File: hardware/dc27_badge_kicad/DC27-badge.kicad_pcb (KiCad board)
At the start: 4 copper layers, 79.1 x 184.5 mm, 141 parts, among them J101 Conn_ARM_JTAG_SWD_10, J102 ShittyAddOnL, J103 ShittyAddOnR, J104 Conn_02x20_Odd_Even, J601 USB_MICRO_RIGHT, Q401 FDN360P, SW108 RESET, SW401 POWER ON, SW801 SKRHAAE010, SW802 SKRHAAE010, U100 BMD-340-A-R-DC27-peripheral-c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, U301 IS31FL3216A, U401 MCP73833, U402 LM1117-3.3, U501 CS4344-CZZ, U502 LM4880, U601 CP2102N-A01-GQFN28, U602 TPD3E001DRLR, Y101 32.768Khz XTAL

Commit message: update gerbers for R302 issue
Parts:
- H701: value MountingHole-Mechanical -> Bomb Face
- R302: footprint Resistor_SMD:R_0603_1608Metric -> Resistor_SMD:R_0805_2012Metric
- U301: value IS31FL3216A -> IS31FL3736-QFLS4-TR
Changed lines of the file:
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@@
     (add_net ~RESET_TGTMCU)
   )
+  (module Resistor_SMD:R_0805_2012Metric (layer F.Cu)
+    (at 108.5125 200)
+    (descr "Resistor SMD 0805 (2012 Metric), square (rectangular) end terminal, IPC_7351 nominal, (Body size source: https://docs.google.com/spreadsheets/d/1BsfQQcO9C6DZCsRaXUlFlo91Tg2WpOkGARC1WS5S8t0/edit?usp=sharing), generated with kicad-footprint-generator")
+    (tags resistor)
+    (attr smd)
+    (fp_text reference R302 (at 0 -1.65) (layer F.SilkS)
+      (effects (font (size 1 1) (thickness 0.15)))
+    )
+    (fp_text value 20K (at 0 1.65) (layer F.Fab)
+      (effects (font (size 1 1) (thickness 0.15)))
+    )
+    (fp_text user %R (at 0 0) (layer F.Fab)
+      (effects (font (size 0.5 0.5) (thickness 0.08)))
+    )
+    (fp_line (start 1.68 0.95) (end -1.68 0.95) (layer F.CrtYd) (width 0.05))
+    (fp_line (start 1.68 -0.95) (end 1.68 0.95) (layer F.CrtYd) (width 0.05))
+    (fp_line (start -1.68 -0.95) (end 1.68 -0.95) (layer F.CrtYd) (width 0.05))
+    (fp_line (start -1.68 0.95) (end -1.68 -0.95) (layer F.CrtYd) (width 0.05))
+    (fp_line (start -0.258578 0.71) (end 0.258578 0.71) (layer F.SilkS) (width 0.12))
+    (fp_line (start -0.258578 -0.71) (end 0.258578 -0.71) (layer F.SilkS) (width 0.12))
+    (fp_line (start 1 0.6) (end -1 0.6) (layer F.Fab) (width 0.1))
+    (fp_line (start 1 -0.6) (end 1 0.6) (layer F.Fab) (width 0.1))
+    (fp_line (start -1 -0.6) (end 1 -0.6) (layer F.Fab) (width 0.1))
+    (fp_line (start -1 0.6) (end -1 -0.6) (layer F.Fab) (width 0.1))
+    (pad 2 smd roundrect (at 0.9375 0) (size 0.975 1.4) (layers F.Cu F.Paste F.Mask) (roundrect_rratio 0.25)
+      (net 58 "Net-(R302-Pad2)"))
+    (pad 1 smd roundrect (at -0.9375 0) (size 0.975 1.4) (layers F.Cu F.Paste F.Mask) (roundrect_rratio 0.25)
+      (net 138 GND))
+    (model ${KISYS3DMOD}/Resistor_SMD.3dshapes/R_0805_2012Metric.wrl
+      (at (xyz 0 0 0))
+      (scale (xyz 1 1 1))
+      (rotate (xyz 0 0 0))
+    )
+  )
   (module lib_fp:bombface-moved (layer F.Cu)
     (at 105.15 201.5)
@@
       (effects (font (size 1.524 1.524) (thickness 0.3)))
     )
-    (fp_text value MountingHole-Mechanical (at 0.75 0) (layer F.SilkS) hide
+    (fp_text value "Bomb Face" (at 0.75 0) (layer F.SilkS) hide
       (effects (font (size 1.524 1.524) (thickness 0.3)))
     )
@@
       (effects (font (size 1 1) (thickness 0.15)))
     )
-    (fp_text value IS31FL3216A (at 0 3.875 180) (layer F.Fab)
+    (fp_text value IS31FL3736-QFLS4-TR (at 0 3.875 180) (layer F.Fab)
       (effects (font (size 1 1) (thickness 0.15)))
     )
@@
   )
   (module Resistor_SMD:R_0603_1608Metric (layer F.Cu)
-    (at 108.5125 200)
-    (descr "Resistor SMD 0603 (1608 Metric), square (rectangular) end terminal, IPC_7351 nominal, (Body size source: http://www.tortai-tech.com/upload/download/2011102023233369053.pdf), generated with kicad-footprint-generator")
-    (tags resistor)
-    (attr smd)
-    (fp_text reference R302 (at 0 -1.43) (layer F.SilkS)
-      (effects (font (size 1 1) (thickness 0.15)))
-    )
-    (fp_text value 20K (at 0 1.43) (layer F.Fab)
-      (effects (font (size 1 1) (thickness 0.15)))
-    )
-    (fp_text user %R (at 0 0) (layer F.Fab)
-      (effects (font (size 0.4 0.4) (thickness 0.06)))
-    )
-    (fp_line (start 1.48 0.73) (end -1.48 0.73) (layer F.CrtYd) (width 0.05))
-    (fp_line (start 1.48 -0.73) (end 1.48 0.73) (layer F.CrtYd) (width 0.05))
-    (fp_line (start -1.48 -0.73) (end 1.48 -0.73) (layer F.CrtYd) (width 0.05))
-    (fp_line (start -1.48 0.73) (end -1.48 -0.73) (layer F.CrtYd) (width 0.05))
-    (fp_line (start -0.162779 0.51) (end 0.162779 0.51) (layer F.SilkS) (width 0.12))
-    (fp_line (start -0.162779 -0.51) (end 0.162779 -0.51) (layer F.SilkS) (width 0.12))
-    (fp_line (start 0.8 0.4) (end -0.8 0.4) (layer F.Fab) (width 0.1))
-    (fp_line (start 0.8 -0.4) (end 0.8 0.4) (layer F.Fab) (width 0.1))
-    (fp_line (start -0.8 -0.4) (end 0.8 -0.4) (layer F.Fab) (width 0.1))
-    (fp_line (start -0.8 0.4) (end -0.8 -0.4) (layer F.Fab) (width 0.1))
-    (pad 2 smd roundrect (at 0.7875 0) (size 0.875 0.95) (layers F.Cu F.Paste F.Mask) (roundrect_rratio 0.25)
-      (net 58 "Net-(R302-Pad2)"))
-    (pad 1 smd roundrect (at -0.7875 0) (size 0.875 0.95) (layers F.Cu F.Paste F.Mask) (roundrect_rratio 0.25)
-      (net 138 GND))
-    (model ${KISYS3DMOD}/Resistor_SMD.3dshapes/R_0603_1608Metric.wrl
-      (at (xyz 0 0 0))
-      (scale (xyz 1 1 1))
-      (rotate (xyz 0 0 0))
-    )
-  )
-  (module Resistor_SMD:R_0603_1608Metric (layer F.Cu)
     (at 90.86 140.655)
     (descr "Resistor SMD 0603 (1608 Metric), square (rectangular) end terminal, IPC_7351 nominal, (Body size source: http://www.tortai-tech.com/upload/download/2011102023233369053.pdf), generated with kicad-footprint-generator")
@@
   (segment (start 110.66509 199.13) (end 110.6 199.06491) (width 0.1524) (layer F.Cu) (net 1))
   (segment (start 112.17 199.13) (end 110.66509 199.13) (width 0.1524) (layer F.Cu) (net 1) (status 10))
-  (segment (start 108.58629 200.79879) (end 109.6 201.8125) (width 0.1524) (layer F.Cu) (net 1) (status 20))
-  (segment (start 108.58629 199.538728) (end 108.58629 200.79879) (width 0.1524) (layer F.Cu) (net 1))
-  (segment (start 109.060108 199.06491) (end 108.58629 199.538728) (width 0.1524) (layer F.Cu) (net 1))
-  (segment (start 110.6 199.06491) (end 109.060108 199.06491) (width 0.1524) (layer F.Cu) (net 1))
   (segment (start 109.461612 191.138388) (end 109 191.6) (width 0.1524) (layer F.Cu) (net 1) (status 20))
   (segment (start 109.461612 188.350888) (end 109.461612 191.138388) (width 0.1524) (layer F.Cu) (net 1))
@@
   (segment (start 81.947044 123.512404) (end 79.05482 120.62018) (width 0.254) (layer B.Cu) (net 1))
   (segment (start 81.64 136.872952) (end 81.947044 136.565908) (width 0.254) (layer B.Cu) (net 1))
+  (segment (start 108.78649 199.369878) (end 108.78649 201.08649) (width 0.152) (layer F.Cu) (net 1))
+  (segment (start 109.091458 199.06491) (end 108.78649 199.369878) (width 0.152) (layer F.Cu) (net 1))
+  (segment (start 110.6 199.06491) (end 109.091458 199.06491) (width 0.152) (layer F.Cu) (net 1))
+  (segment (start 108.78649 201.08649) (end 109.5 201.8) (width 0.152) (layer F.Cu) (net 1))
   (via (at 102.01 98.77) (size 0.6) (drill 0.4) (layers F.Cu B.Cu) (net 2))
   (segment (start 102.2 98.96) (end 102.01 98.77) (width 0.1524) (layer F.Cu) (net 2))

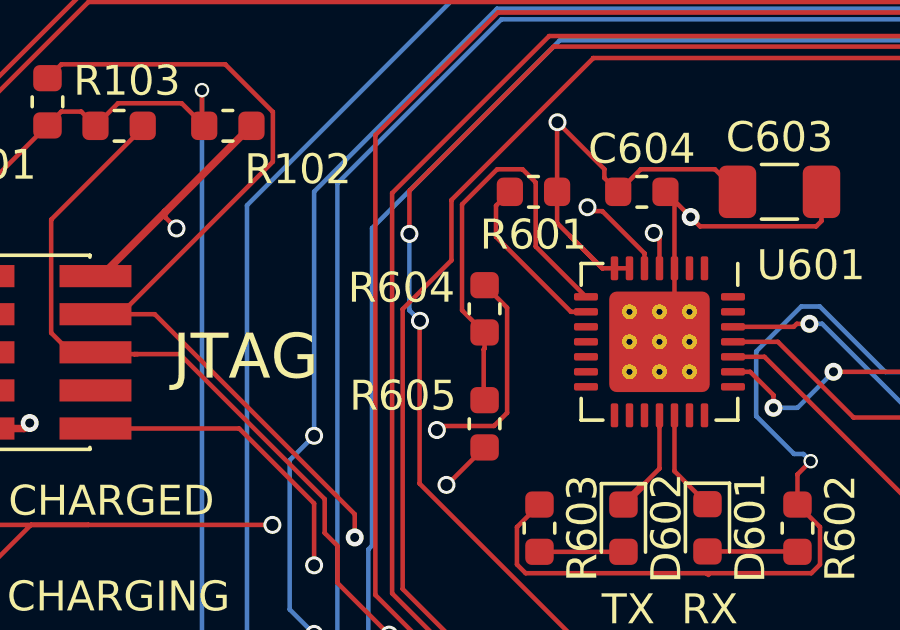
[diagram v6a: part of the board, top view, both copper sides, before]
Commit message: Fix R604 and other dumb 0603/0805 mistakes
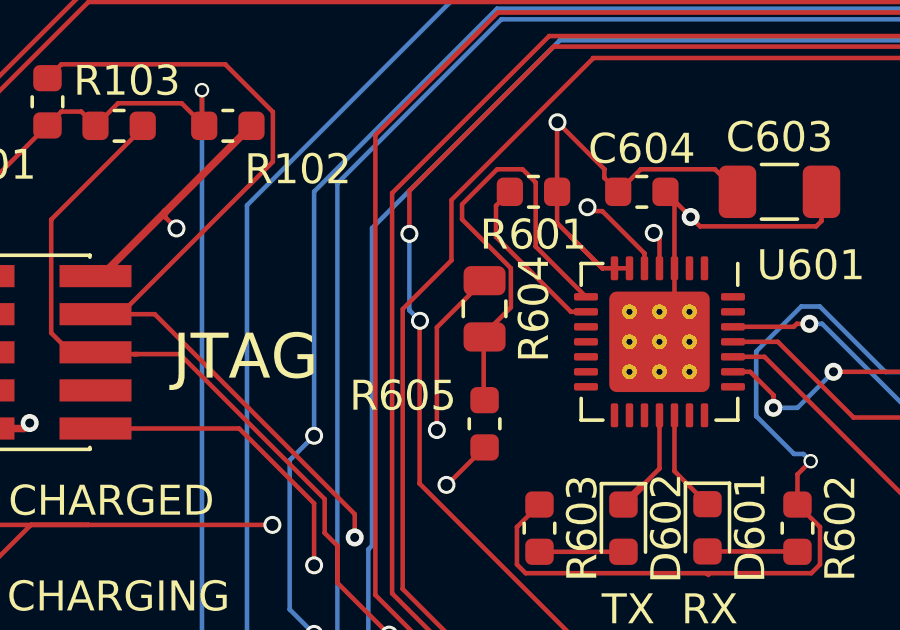
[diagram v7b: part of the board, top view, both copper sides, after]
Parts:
- R604: footprint Resistor_SMD:R_0603_1608Metric -> Resistor_SMD:R_0805_2012Metric
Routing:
- net VBUS: track 116.6 -> 115.2 mm
- net Net-(R604-Pad2): track 14.5 -> 15.1 mm
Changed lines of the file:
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@@
   )
   (module Resistor_SMD:R_0805_2012Metric (layer F.Cu)
+    (at 96.37 101.3 270)
+    (descr "Resistor SMD 0805 (2012 Metric), square (rectangular) end terminal, IPC_7351 nominal, (Body size source: https://docs.google.com/spreadsheets/d/1BsfQQcO9C6DZCsRaXUlFlo91Tg2WpOkGARC1WS5S8t0/edit?usp=sharing), generated with kicad-footprint-generator")
+    (tags resistor)
+    (attr smd)
+    (fp_text reference R604 (at 0 -1.65 270) (layer F.SilkS)
+      (effects (font (size 1 1) (thickness 0.15)))
+    )
+    (fp_text value 22.1k (at 0 1.65 270) (layer F.Fab)
+      (effects (font (size 1 1) (thickness 0.15)))
+    )
+    (fp_text user %R (at 0 0 270) (layer F.Fab)
+      (effects (font (size 0.5 0.5) (thickness 0.08)))
+    )
+    (fp_line (start 1.68 0.95) (end -1.68 0.95) (layer F.CrtYd) (width 0.05))
+    (fp_line (start 1.68 -0.95) (end 1.68 0.95) (layer F.CrtYd) (width 0.05))
+    (fp_line (start -1.68 -0.95) (end 1.68 -0.95) (layer F.CrtYd) (width 0.05))
+    (fp_line (start -1.68 0.95) (end -1.68 -0.95) (layer F.CrtYd) (width 0.05))
+    (fp_line (start -0.258578 0.71) (end 0.258578 0.71) (layer F.SilkS) (width 0.12))
+    (fp_line (start -0.258578 -0.71) (end 0.258578 -0.71) (layer F.SilkS) (width 0.12))
+    (fp_line (start 1 0.6) (end -1 0.6) (layer F.Fab) (width 0.1))
+    (fp_line (start 1 -0.6) (end 1 0.6) (layer F.Fab) (width 0.1))
+    (fp_line (start -1 -0.6) (end 1 -0.6) (layer F.Fab) (width 0.1))
+    (fp_line (start -1 0.6) (end -1 -0.6) (layer F.Fab) (width 0.1))
+    (pad 2 smd roundrect (at 0.9375 0 270) (size 0.975 1.4) (layers F.Cu F.Paste F.Mask) (roundrect_rratio 0.25)
+      (net 54 "Net-(R604-Pad2)"))
+    (pad 1 smd roundrect (at -0.9375 0 270) (size 0.975 1.4) (layers F.Cu F.Paste F.Mask) (roundrect_rratio 0.25)
+      (net 32 VBUS))
+    (model ${KISYS3DMOD}/Resistor_SMD.3dshapes/R_0805_2012Metric.wrl
+      (at (xyz 0 0 0))
+      (scale (xyz 1 1 1))
+      (rotate (xyz 0 0 0))
+    )
+  )
+  (module Resistor_SMD:R_0805_2012Metric (layer F.Cu)
     (at 108.5125 200)
     (descr "Resistor SMD 0805 (2012 Metric), square (rectangular) end terminal, IPC_7351 nominal, (Body size source: https://docs.google.com/spreadsheets/d/1BsfQQcO9C6DZCsRaXUlFlo91Tg2WpOkGARC1WS5S8t0/edit?usp=sharing), generated with kicad-footprint-generator")
@@
   )
   (module Resistor_SMD:R_0603_1608Metric (layer F.Cu)
-    (at 96.37 101.3 270)
-    (descr "Resistor SMD 0603 (1608 Metric), square (rectangular) end terminal, IPC_7351 nominal, (Body size source: http://www.tortai-tech.com/upload/download/2011102023233369053.pdf), generated with kicad-footprint-generator")
-    (tags resistor)
-    (attr smd)
-    (fp_text reference R604 (at -0.7 2.77) (layer F.SilkS)
-      (effects (font (size 1 1) (thickness 0.15)))
-    )
-    (fp_text value 22.1k (at 0 1.43 270) (layer F.Fab)
-      (effects (font (size 1 1) (thickness 0.15)))
-    )
-    (fp_text user %R (at 0 0 270) (layer F.Fab)
-      (effects (font (size 0.4 0.4) (thickness 0.06)))
-    )
-    (fp_line (start 1.48 0.73) (end -1.48 0.73) (layer F.CrtYd) (width 0.05))
-    (fp_line (start 1.48 -0.73) (end 1.48 0.73) (layer F.CrtYd) (width 0.05))
-    (fp_line (start -1.48 -0.73) (end 1.48 -0.73) (layer F.CrtYd) (width 0.05))
-    (fp_line (start -1.48 0.73) (end -1.48 -0.73) (layer F.CrtYd) (width 0.05))
-    (fp_line (start -0.162779 0.51) (end 0.162779 0.51) (layer F.SilkS) (width 0.12))
-    (fp_line (start -0.162779 -0.51) (end 0.162779 -0.51) (layer F.SilkS) (width 0.12))
-    (fp_line (start 0.8 0.4) (end -0.8 0.4) (layer F.Fab) (width 0.1))
-    (fp_line (start 0.8 -0.4) (end 0.8 0.4) (layer F.Fab) (width 0.1))
-    (fp_line (start -0.8 -0.4) (end 0.8 -0.4) (layer F.Fab) (width 0.1))
-    (fp_line (start -0.8 0.4) (end -0.8 -0.4) (layer F.Fab) (width 0.1))
-    (pad 2 smd roundrect (at 0.7875 0 270) (size 0.875 0.95) (layers F.Cu F.Paste F.Mask) (roundrect_rratio 0.25)
-      (net 54 "Net-(R604-Pad2)"))
-    (pad 1 smd roundrect (at -0.7875 0 270) (size 0.875 0.95) (layers F.Cu F.Paste F.Mask) (roundrect_rratio 0.25)
-      (net 32 VBUS))
-    (model ${KISYS3DMOD}/Resistor_SMD.3dshapes/R_0603_1608Metric.wrl
-      (at (xyz 0 0 0))
-      (scale (xyz 1 1 1))
-      (rotate (xyz 0 0 0))
-    )
-  )
-  (module Resistor_SMD:R_0603_1608Metric (layer F.Cu)
     (at 98.2 108.612 270)
     (descr "Resistor SMD 0603 (1608 Metric), square (rectangular) end terminal, IPC_7351 nominal, (Body size source: http://www.tortai-tech.com/upload/download/2011102023233369053.pdf), generated with kicad-footprint-generator")
@@
   (segment (start 109.14 116.774) (end 109.14 116.17399) (width 0.1524) (layer F.Cu) (net 25) (status 30))
   (segment (start 97.999999 115) (end 93.64 110.640001) (width 0.1524) (layer F.Cu) (net 25))
-  (segment (start 93.64 101.31) (end 95.26638 99.68362) (width 0.1524) (layer F.Cu) (net 25))
   (segment (start 93.64 110.640001) (end 93.64 101.31) (width 0.1524) (layer F.Cu) (net 25))
   (segment (start 99.99 92.949135) (end 99.99 92.94) (width 0.1524) (layer F.Cu) (net 25))
-  (segment (start 95.26638 99.68362) (end 95.26638 97.672755) (width 0.1524) (layer F.Cu) (net 25))
   (segment (start 95.26638 97.672755) (end 99.99 92.949135) (width 0.1524) (layer F.Cu) (net 25))
   (segment (start 122.58 92.94) (end 99.99 92.94) (width 0.1524) (layer F.Cu) (net 25))
+  (segment (start 95.26638 99.68362) (end 93.64 101.31) (width 0.152) (layer F.Cu) (net 25))
+  (segment (start 95.26638 97.672755) (end 95.26638 99.68362) (width 0.152) (layer F.Cu) (net 25))
   (segment (start 96.34969 114.478688) (end 96.34969 114.45969) (width 0.1524) (layer F.Cu) (net 26))
   (segment (start 96.34969 114.45969) (end 92.73 110.84) (width 0.1524) (layer F.Cu) (net 26))
@@
   (via (at 94.78 105.34) (size 0.6) (drill 0.4) (layers F.Cu B.Cu) (net 32))
   (segment (start 94.91371 105.20629) (end 94.78 105.34) (width 0.1524) (layer F.Cu) (net 32))
-  (segment (start 97.12121 104.768772) (end 96.683692 105.20629) (width 0.1524) (layer F.Cu) (net 32))
-  (segment (start 97.12121 101.26371) (end 97.12121 104.768772) (width 0.1524) (layer F.Cu) (net 32))
-  (segment (start 96.683692 105.20629) (end 94.91371 105.20629) (width 0.1524) (layer F.Cu) (net 32))
-  (segment (start 96.37 100.5125) (end 97.12121 101.26371) (width 0.1524) (layer F.Cu) (net 32) (status 10))
   (via (at 89.297435 108.502565) (size 0.6) (drill 0.4) (layers F.Cu B.Cu) (net 32))
   (segment (start 92.46 105.34) (end 89.297435 108.502565) (width 0.1524) (layer PWR) (net 32))
@@
   (segment (start 80.85621 135.17579) (end 81.402 134.63) (width 0.254) (layer F.Cu) (net 32))
   (segment (start 80.85621 135.56958) (end 80.85621 135.17579) (width 0.254) (layer F.Cu) (net 32))
+  (segment (start 94.78 105.34) (end 94.78 101.92) (width 0.152) (layer F.Cu) (net 32))
+  (segment (start 94.78 101.92) (end 96.3 100.4) (width 0.152) (layer F.Cu) (net 32))
   (segment (start 67.6973 174.66) (end 67.5847 174.5474) (width 0.25) (layer F.Cu) (net 33))
   (segment (start 67.5847 174.5474) (end 67.5847 169.66) (width 0.25) (layer F.Cu) (net 33))
@@
   (segment (start 96.37 102.0875) (end 96.37 102.625) (width 0.1524) (layer F.Cu) (net 54) (status 10))
   (segment (start 96.34 102.655) (end 96.34 104.32) (width 0.1524) (layer F.Cu) (net 54) (status 20))
-  (segment (start 95.61879 97.818728) (end 95.61879 101.34879) (width 0.1524) (layer F.Cu) (net 54))
   (segment (start 98.07379 99.22379) (end 98.07379 97.086308) (width 0.1524) (layer F.Cu) (net 54))
   (segment (start 96.788728 96.64879) (end 95.61879 97.818728) (width 0.1524) (layer F.Cu) (net 54))
@@
   (segment (start 97.636272 96.64879) (end 96.788728 96.64879) (width 0.1524) (layer F.Cu) (net 54))
   (segment (start 98.07379 97.086308) (end 97.636272 96.64879) (width 0.1524) (layer F.Cu) (net 54))
-  (segment (start 95.61879 101.34879) (end 96.37 102.1) (width 0.1524) (layer F.Cu) (net 54) (status 20))
+  (segment (start 97.24601 99.944878) (end 97.24601 101.25399) (width 0.152) (layer F.Cu) (net 54))
+  (segment (start 95.61879 98.317658) (end 97.24601 99.944878) (width 0.152) (layer F.Cu) (net 54))
+  (segment (start 95.61879 97.818728) (end 95.61879 98.317658) (width 0.152) (layer F.Cu) (net 54))
+  (segment (start 97.24601 101.25399) (end 96.425 102.075) (width 0.152) (layer F.Cu) (net 54))
   (segment (start 101.94 49.345) (end 102.91621 50.32121) (width 0.1524) (layer B.Cu) (net 55) (status 10))
   (segment (start 102.91621 51.685406) (end 101.974027 52.627589) (width 0.1524) (layer B.Cu) (net 55))
